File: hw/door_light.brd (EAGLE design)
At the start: 32.2 x 33.6 mm, 28 parts, among them IC1 TINY13-20SSU, J1 PWR, J2 LIGHT, Q1 BSP250, T2 KP-3216P3C, U1 MC33063ADE4

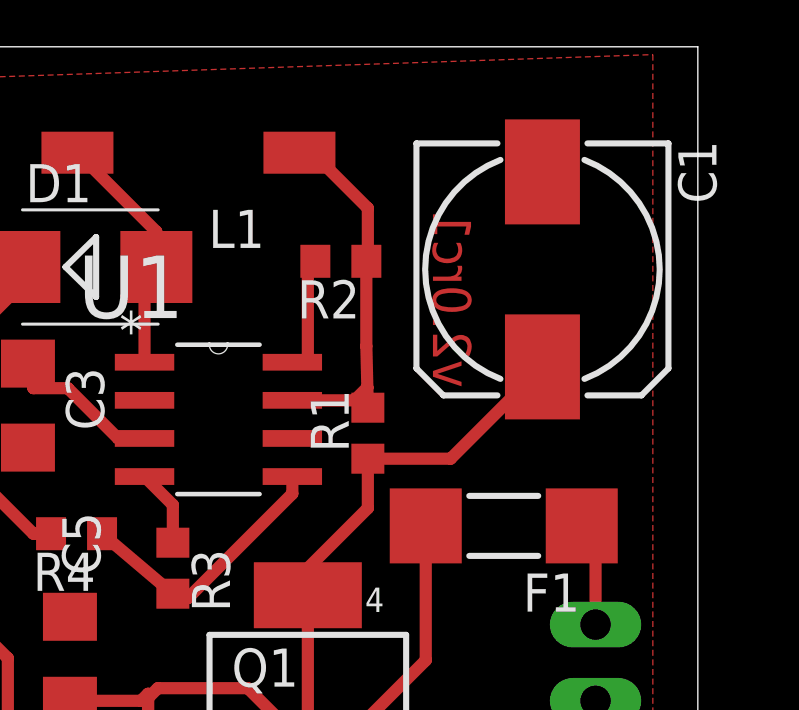
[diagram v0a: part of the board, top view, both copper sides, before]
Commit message: fixed resistor voltage divider
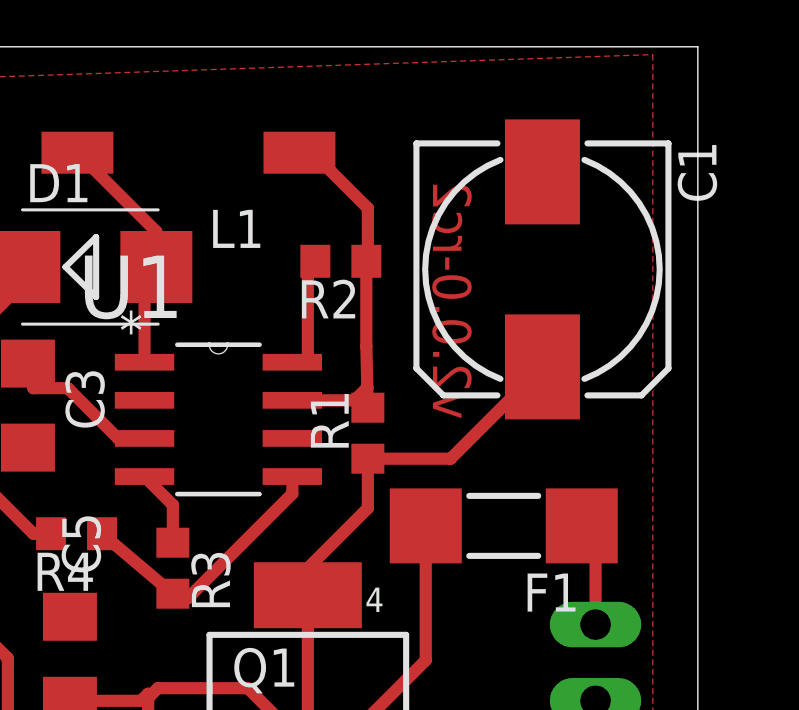
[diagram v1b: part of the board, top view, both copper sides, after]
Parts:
- R11: value 2.4kR -> 2.9kR
- R8: value 2.4kR -> 10kR
- R9: value 10kR -> 2.9kR
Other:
- board text added: "v2.0.0-rc2"
- board text removed: "v2.0rc1"
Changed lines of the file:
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@@
 <layer number="23" name="tOrigins" color="15" fill="1" visible="yes" active="yes"/>
 <layer number="24" name="bOrigins" color="15" fill="1" visible="yes" active="yes"/>
-<layer number="25" name="tNames" color="7" fill="1" visible="yes" active="yes"/>
-<layer number="26" name="bNames" color="7" fill="1" visible="yes" active="yes"/>
-<layer number="27" name="tValues" color="7" fill="1" visible="yes" active="yes"/>
-<layer number="28" name="bValues" color="7" fill="1" visible="yes" active="yes"/>
+<layer number="25" name="tNames" color="7" fill="1" visible="no" active="yes"/>
+<layer number="26" name="bNames" color="7" fill="1" visible="no" active="yes"/>
+<layer number="27" name="tValues" color="7" fill="1" visible="no" active="yes"/>
+<layer number="28" name="bValues" color="7" fill="1" visible="no" active="yes"/>
 <layer number="29" name="tStop" color="7" fill="3" visible="no" active="yes"/>
 <layer number="30" name="bStop" color="7" fill="6" visible="no" active="yes"/>
@@
 <wire x1="50" y1="73.38" x2="17.78" y2="73.38" width="0" layer="20"/>
 <wire x1="17.78" y1="73.38" x2="17.78" y2="39.75" width="0" layer="20"/>
-<text x="42.44" y="67.94" size="1.27" layer="1" rot="MR270">v2.0rc1</text>
+<text x="42.44" y="68.94" size="1.27" layer="1" rot="MR270">v2.0.0-rc2</text>
 </plain>
 <attributes>
@@
 <element name="R4" library="rcl" package="R0603" value="24kR" x="29.29" y="57.15" rot="R180"/>
 <element name="R3" library="rcl" package="R0603" value="2.7kR" x="32.5" y="56" rot="R270"/>
-<element name="R9" library="rcl" package="R0603" value="10kR" x="27" y="43"/>
+<element name="R9" library="rcl" package="R0603" value="2.9kR" x="27" y="43"/>
 <element name="R10" library="rcl" package="R0603" value="10kR" x="23.33" y="50.01"/>
-<element name="R8" library="rcl" package="R0603" value="2.4kR" x="31" y="43"/>
-<element name="R11" library="rcl" package="R0603" value="2.4kR" x="23" y="44.5" rot="R90"/>
+<element name="R8" library="rcl" package="R0603" value="10kR" x="31" y="43"/>
+<element name="R11" library="rcl" package="R0603" value="2.9kR" x="23" y="44.5" rot="R90"/>
 <element name="LED2" library="led" package="CHIPLED_0805" value="IR" x="43.72" y="44.45" rot="R180"/>
 <element name="LED1" library="led" package="CHIPLED_0603" value="RED" x="43.72" y="48.26"/>

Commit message: pads for power and LED connecting are now SMD as well
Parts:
- removed J1: PWR, con-amp:10X02MTA
- removed J2: LIGHT, con-amp:10X02MTA
- added SJ1: PWR, jumper:SJW
- added SJ2: LIGHT, jumper:SJW
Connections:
- net +12V: now also SJ2.2; no longer J2.2
- net 0V: now also SJ1.1, SJ2.1; no longer J1.1, J2.1
- net N$8: now also SJ1.2; no longer J1.2
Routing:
- net +12V: track 20.4 -> 22.2 mm
- net N$8: track 3.48 -> 4.66 mm
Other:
- board text added: "LED"
- board text added: "P"
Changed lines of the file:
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@@
 <wire x1="17.78" y1="73.38" x2="17.78" y2="39.75" width="0" layer="20"/>
 <text x="42.44" y="68.94" size="1.27" layer="1" rot="MR270">v2.0.0-rc2</text>
+<text x="24" y="66.5" size="1.016" layer="1">P</text>
+<text x="48.5" y="55.5" size="1.016" layer="1" rot="R90">LED</text>
 </plain>
 <attributes>
@@
 <attribute name="VALUE" x="29.324" y="45.614" size="1.27" layer="27" ratio="10" rot="R90"/>
 </element>
-<element name="J1" library="con-amp" package="10X02MTA" value="PWR" x="46.59" y="52.85" smashed="yes" rot="MR270">
-<attribute name="NAME" x="49.2062" y="52.1388" size="1.27" layer="26" rot="MR0"/>
-<attribute name="VALUE" x="44.4391" y="55.3961" size="1.27" layer="28" rot="MR270"/>
-</element>
-<element name="J2" library="con-amp" package="10X02MTA" value="LIGHT" x="21.88" y="68.72" rot="MR0"/>
 <element name="C2" library="rcl" package="C1206" value="100nF" x="23.67" y="52.07" smashed="yes" rot="R180">
 <attribute name="NAME" x="22.146" y="50.546" size="1.27" layer="25" ratio="10" rot="R180"/>
@@
 <attribute name="OC_FARNELL" value="unknown" x="37" y="44" size="1.778" layer="27" rot="R90" display="off"/>
 </element>
+<element name="SJ1" library="jumper" package="SJW" value="PWR" x="47" y="53" rot="R90"/>
+<element name="SJ2" library="jumper" package="SJW" value="LIGHT" x="23" y="69.5" rot="R180"/>
 </elements>
 <signals>
@@
 <contactref element="IC1" pad="4"/>
 <contactref element="C5" pad="2"/>
-<contactref element="J1" pad="1"/>
 <contactref element="C2" pad="2"/>
 <polygon width="0.6096" layer="1" isolate="0.6096" orphans="yes">
@@
 <contactref element="R11" pad="1"/>
 <contactref element="T2" pad="EMITER"/>
-<contactref element="J2" pad="1"/>
 <contactref element="T1" pad="2"/>
 <wire x1="32.5" y1="56.85" x2="32.5" y2="58.1112" width="0.4064" layer="1"/>
@@
 <wire x1="26.15" y1="43" x2="27" y2="44.461" width="0.4064" layer="1"/>
 <wire x1="27" y1="44.461" x2="26.366" y2="45.095" width="0.4064" layer="1"/>
+<contactref element="SJ2" pad="1"/>
+<contactref element="SJ1" pad="1"/>
 </signal>
 <signal name="+12V">
-<contactref element="J2" pad="2"/>
 <contactref element="D1" pad="C"/>
 <contactref element="C4" pad="+"/>
 <contactref element="R4" pad="2"/>
-<wire x1="27.55" y1="66.04" x2="25.83" y2="66.04" width="0.4064" layer="1"/>
-<wire x1="25.83" y1="66.04" x2="23.15" y2="68.72" width="0.4064" layer="1"/>
 <wire x1="21.86" y1="65.29" x2="21.86" y2="66.86" width="0.4064" layer="1"/>
-<wire x1="21.86" y1="66.86" x2="23" y2="68" width="0.4064" layer="1"/>
-<wire x1="23" y1="68" x2="23" y2="68.57" width="0.4064" layer="1"/>
-<wire x1="23" y1="68.57" x2="23.15" y2="68.72" width="0.4064" layer="1"/>
-<wire x1="27.55" y1="65.55" x2="26" y2="64" width="0.4064" layer="1"/>
+<wire x1="27.55" y1="65.55" x2="27" y2="65" width="0.4064" layer="1"/>
+<wire x1="27" y1="65" x2="26" y2="64" width="0.4064" layer="1"/>
 <wire x1="26" y1="64" x2="26" y2="59" width="0.4064" layer="1"/>
 <wire x1="27.55" y1="65.55" x2="27.55" y2="66.04" width="0.4064" layer="1"/>
 <wire x1="28.44" y1="57.15" x2="27.85" y2="57.15" width="0.4064" layer="1"/>
 <wire x1="27.85" y1="57.15" x2="26" y2="59" width="0.4064" layer="1"/>
+<contactref element="SJ2" pad="2"/>
+<wire x1="21.73" y1="69.5" x2="21.86" y2="69.5" width="0.4064" layer="1"/>
+<wire x1="21.86" y1="69.5" x2="21.86" y2="65.29" width="0.4064" layer="1"/>
+<wire x1="21.86" y1="65.29" x2="27" y2="65.29" width="0.4064" layer="1"/>
+<wire x1="27" y1="65.29" x2="27" y2="65" width="0.4064" layer="1"/>
 </signal>
 <signal name="N$2">
@@
 </signal>
 <signal name="N$8">
-<contactref element="J1" pad="2"/>
 <contactref element="F1" pad="1"/>
-<wire x1="46.59" y1="54.12" x2="46.59" y2="56.95" width="0.4064" layer="1"/>
 <wire x1="46.59" y1="56.95" x2="46.13" y2="57.41" width="0.4064" layer="1"/>
+<contactref element="SJ1" pad="2"/>
+<wire x1="47" y1="54.27" x2="47" y2="57" width="0.4064" layer="1"/>
+<wire x1="47" y1="57" x2="46.13" y2="57" width="0.4064" layer="1"/>
+<wire x1="46.13" y1="57" x2="46.13" y2="57.41" width="0.4064" layer="1"/>
 </signal>
 <signal name="+4.1V">

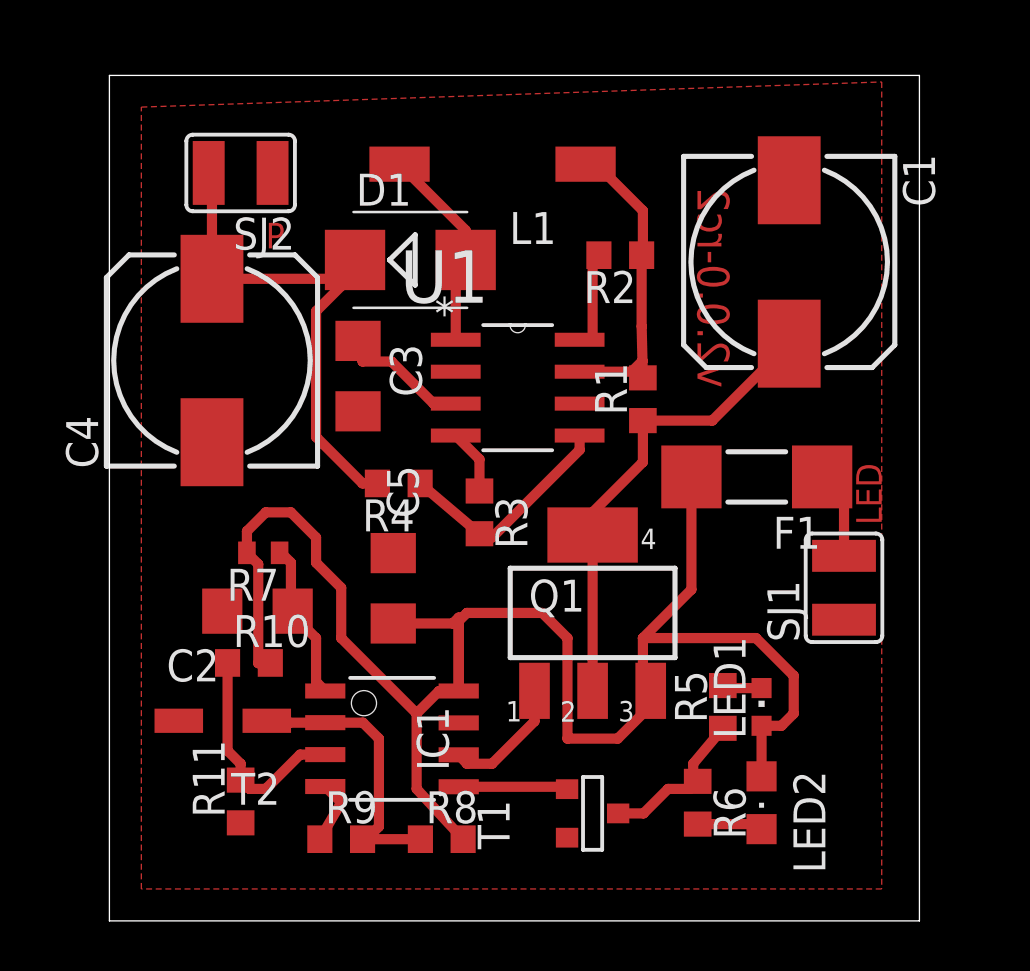
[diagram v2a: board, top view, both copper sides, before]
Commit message: coil type changed (bigger one)
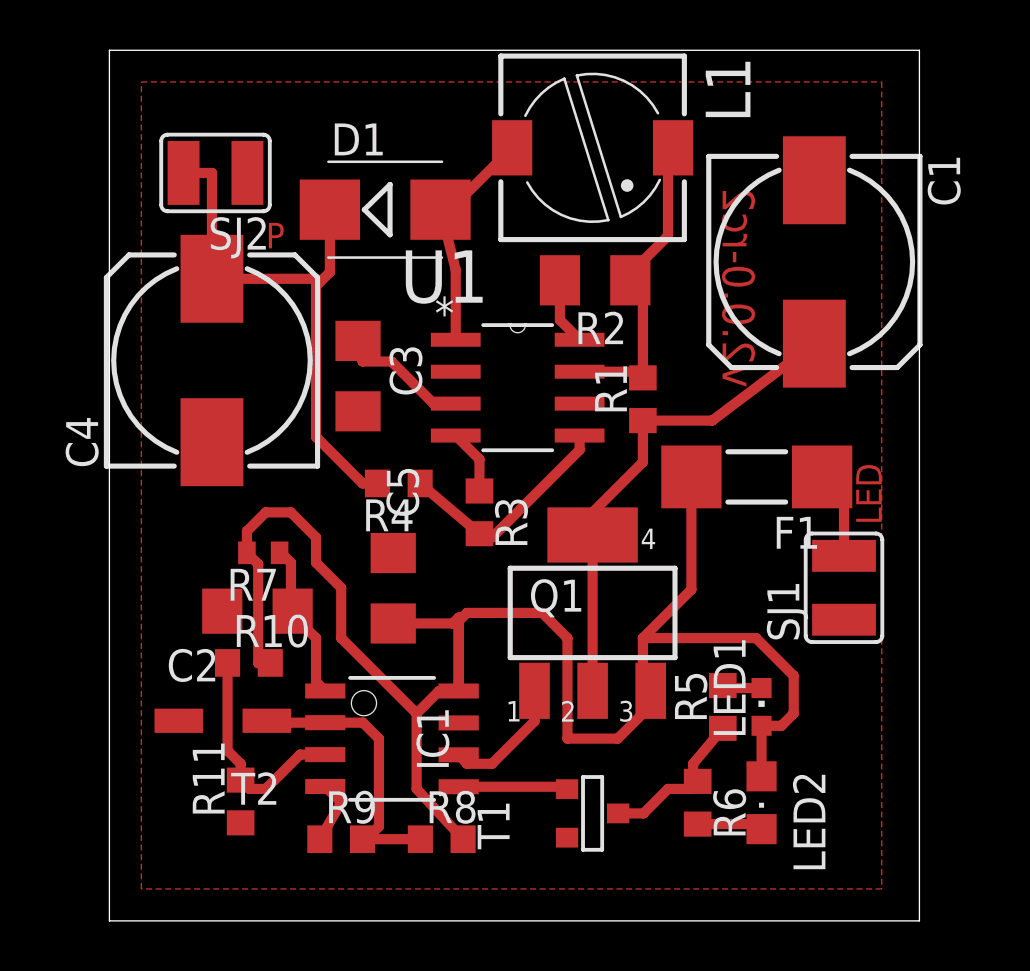
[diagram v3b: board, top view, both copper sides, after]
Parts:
- L1: device rcl:L8530M -> rcl:PIS2816
- R2: device rcl:R0603 -> rcl:M1206
- moved L1 4.03 mm to (37.0, 70.5), turned to 270 degrees
- moved D1 2.24 mm to (28.8, 68.0)
- moved R2 1.41 mm to (37.1, 65.2)
- moved C1 1.00 mm to (45.8, 66.0)
- moved SJ2 1.00 mm to (22.0, 69.5)
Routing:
- net +12V: track 22.2 -> 23.8 mm
- net N$15: track 3.91 -> 2.69 mm
- net N$11: track 8.24 -> 9.12 mm
- net N$3: track 18.7 -> 19.4 mm
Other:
- board size 32.2 x 33.6 mm -> 32.2 x 34.6 mm
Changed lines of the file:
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@@
 <plain>
 <wire x1="17.78" y1="39.75" x2="50" y2="39.75" width="0" layer="20"/>
-<wire x1="50" y1="39.75" x2="50" y2="73.38" width="0" layer="20"/>
-<wire x1="50" y1="73.38" x2="17.78" y2="73.38" width="0" layer="20"/>
-<wire x1="17.78" y1="73.38" x2="17.78" y2="39.75" width="0" layer="20"/>
-<text x="42.44" y="68.94" size="1.27" layer="1" rot="MR270">v2.0.0-rc2</text>
+<wire x1="50" y1="39.75" x2="50" y2="74.38" width="0" layer="20"/>
+<wire x1="50" y1="74.38" x2="17.78" y2="74.38" width="0" layer="20"/>
+<wire x1="17.78" y1="74.38" x2="17.78" y2="39.75" width="0" layer="20"/>
+<text x="43.44" y="68.94" size="1.27" layer="1" rot="MR270">v2.0.0-rc2</text>
 <text x="24" y="66.5" size="1.016" layer="1">P</text>
 <text x="48.5" y="55.5" size="1.016" layer="1" rot="R90">LED</text>
@@
 <element name="F1" library="rcl" package="MINI_MELF-0207W" value="1206L035YR (F750mA)" x="43.53" y="57.41" rot="R180"/>
 <element name="R7" library="rcl" package="R0402" value="10kR" x="23.9" y="54.39" rot="R180"/>
-<element name="D1" library="diode" package="SMB" value=" MBRS140T3G" x="29.75" y="66.04"/>
+<element name="D1" library="diode" package="SMB" value=" MBRS140T3G" x="28.75" y="68.04"/>
 <element name="C3" library="rcl" package="C1206" value="1.5nF" x="27.67" y="61.42" rot="R270"/>
-<element name="C1" library="rcl" package="153CLV-0810" value="100uF" x="44.82" y="65.96" rot="R270"/>
+<element name="C1" library="rcl" package="153CLV-0810" value="100uF" x="45.82" y="65.96" rot="R270"/>
 <element name="C4" library="rcl" package="153CLV-0810" value="100uF" x="21.86" y="62.04" rot="R90"/>
-<element name="L1" library="rcl" package="L8530M" value="150uH" x="33.02" y="69.85" rot="R180"/>
-<element name="R2" library="rcl" package="R0603" value="180R" x="38.1" y="66.23" rot="R180"/>
+<element name="L1" library="rcl" package="PIS2816" value="150uH" x="37" y="70.5" rot="R270"/>
+<element name="R2" library="rcl" package="M1206" value="180R" x="37.1" y="65.23" rot="R180"/>
 <element name="R1" library="rcl" package="R0603" value="0.22R" x="39" y="60.5" rot="R90"/>
 <element name="R4" library="rcl" package="R0603" value="24kR" x="29.29" y="57.15" rot="R180"/>
@@
 </element>
 <element name="SJ1" library="jumper" package="SJW" value="PWR" x="47" y="53" rot="R90"/>
-<element name="SJ2" library="jumper" package="SJW" value="LIGHT" x="23" y="69.5" rot="R180"/>
+<element name="SJ2" library="jumper" package="SJW" value="LIGHT" x="22" y="69.5" rot="R180"/>
 </elements>
 <signals>
@@
 <polygon width="0.6096" layer="1" isolate="0.6096" orphans="yes">
 <vertex x="19.05" y="41.02"/>
-<vertex x="19.05" y="72.12"/>
+<vertex x="19.05" y="73.12"/>
 <vertex x="48.5" y="73.12"/>
 <vertex x="48.5" y="41.02"/>
@@
 <contactref element="R4" pad="2"/>
 <wire x1="21.86" y1="65.29" x2="21.86" y2="66.86" width="0.4064" layer="1"/>
-<wire x1="27.55" y1="65.55" x2="27" y2="65" width="0.4064" layer="1"/>
-<wire x1="27" y1="65" x2="26" y2="64" width="0.4064" layer="1"/>
-<wire x1="26" y1="64" x2="26" y2="59" width="0.4064" layer="1"/>
-<wire x1="27.55" y1="65.55" x2="27.55" y2="66.04" width="0.4064" layer="1"/>
+<wire x1="26.55" y1="65.55" x2="26" y2="65" width="0.4064" layer="1"/>
+<wire x1="26" y1="65" x2="26" y2="59" width="0.4064" layer="1"/>
+<wire x1="26.55" y1="65.55" x2="26.55" y2="68.04" width="0.4064" layer="1"/>
 <wire x1="28.44" y1="57.15" x2="27.85" y2="57.15" width="0.4064" layer="1"/>
 <wire x1="27.85" y1="57.15" x2="26" y2="59" width="0.4064" layer="1"/>
 <contactref element="SJ2" pad="2"/>
-<wire x1="21.73" y1="69.5" x2="21.86" y2="69.5" width="0.4064" layer="1"/>
+<wire x1="20.73" y1="69.5" x2="21.86" y2="69.5" width="0.4064" layer="1"/>
 <wire x1="21.86" y1="69.5" x2="21.86" y2="65.29" width="0.4064" layer="1"/>
-<wire x1="21.86" y1="65.29" x2="27" y2="65.29" width="0.4064" layer="1"/>
-<wire x1="27" y1="65.29" x2="27" y2="65" width="0.4064" layer="1"/>
+<wire x1="21.86" y1="65.29" x2="26" y2="65.29" width="0.4064" layer="1"/>
+<wire x1="26" y1="65.29" x2="26" y2="65" width="0.4064" layer="1"/>
 </signal>
 <signal name="N$2">
@@
 <contactref element="L1" pad="2"/>
 <wire x1="31.5562" y1="62.865" x2="31.5562" y2="65.6462" width="0.4064" layer="1"/>
-<wire x1="31.5562" y1="65.6462" x2="31.95" y2="66.04" width="0.4064" layer="1"/>
-<wire x1="31.95" y1="66.04" x2="31.95" y2="67.22" width="0.4064" layer="1"/>
-<wire x1="31.95" y1="67.22" x2="29.32" y2="69.85" width="0.4064" layer="1"/>
+<wire x1="31.5562" y1="65.6462" x2="30.95" y2="68.04" width="0.4064" layer="1"/>
+<wire x1="30.95" y1="68.04" x2="31.34" y2="68.04" width="0.4064" layer="1"/>
+<wire x1="31.34" y1="68.04" x2="33.8" y2="70.5" width="0.4064" layer="1"/>
 </signal>
 <signal name="N$15">
 <contactref element="U1" pad="8"/>
 <contactref element="R2" pad="2"/>
-<wire x1="36.4838" y1="62.865" x2="36.865" y2="62.865" width="0.4064" layer="1"/>
-<wire x1="36.865" y1="62.865" x2="37" y2="63" width="0.4064" layer="1"/>
-<wire x1="37" y1="63" x2="37" y2="65.98" width="0.4064" layer="1"/>
-<wire x1="37" y1="65.98" x2="37.25" y2="66.23" width="0.4064" layer="1"/>
+<wire x1="35.7" y1="65.23" x2="35.7" y2="63.6488" width="0.4064" layer="1"/>
+<wire x1="35.7" y1="63.6488" x2="36.4838" y2="62.865" width="0.4064" layer="1"/>
 </signal>
 <signal name="N$16">
@@
 <contactref element="U1" pad="7"/>
 <contactref element="R1" pad="2"/>
-<wire x1="36.72" y1="69.85" x2="37.15" y2="69.85" width="0.4064" layer="1"/>
-<wire x1="37.15" y1="69.85" x2="39" y2="68" width="0.4064" layer="1"/>
-<wire x1="39" y1="68" x2="39" y2="66.28" width="0.4064" layer="1"/>
-<wire x1="39" y1="66.28" x2="38.95" y2="66.23" width="0.4064" layer="1"/>
-<wire x1="38.95" y1="66.23" x2="38.95" y2="63.4" width="0.4064" layer="1"/>
-<wire x1="38.95" y1="63.4" x2="38.9835625" y2="62.023990625" width="0.4064" layer="1"/>
-<wire x1="38.9835625" y1="62.023990625" x2="39" y2="61.35" width="0.4064" layer="1"/>
 <wire x1="36.4838" y1="61.595" x2="38.554571875" y2="61.595" width="0.4064" layer="1"/>
-<wire x1="38.554571875" y1="61.595" x2="38.9835625" y2="62.023990625" width="0.4064" layer="1"/>
+<wire x1="39" y1="61.35" x2="39" y2="64.73" width="0.4064" layer="1"/>
+<wire x1="39" y1="64.73" x2="38.5" y2="65.23" width="0.4064" layer="1"/>
+<wire x1="38.5" y1="65.23" x2="38.5" y2="65.5" width="0.4064" layer="1"/>
+<wire x1="38.5" y1="65.5" x2="40" y2="67" width="0.4064" layer="1"/>
+<wire x1="40" y1="67" x2="40" y2="70.3" width="0.4064" layer="1"/>
+<wire x1="40" y1="70.3" x2="40.2" y2="70.5" width="0.4064" layer="1"/>
+<wire x1="39" y1="61.35" x2="38.799571875" y2="61.35" width="0.4064" layer="1"/>
+<wire x1="38.799571875" y1="61.35" x2="38.554571875" y2="61.595" width="0.4064" layer="1"/>
 </signal>
 <signal name="N$18">
@@
 <contactref element="C1" pad="+"/>
 <wire x1="39" y1="59.65" x2="41.76" y2="59.65" width="0.4064" layer="1"/>
-<wire x1="41.76" y1="59.65" x2="44.82" y2="62.71" width="0.4064" layer="1"/>
+<wire x1="41.76" y1="59.65" x2="45.82" y2="62.71" width="0.4064" layer="1"/>
 <contactref element="Q1" pad="2"/>
 <contactref element="Q1" pad="4"/>
